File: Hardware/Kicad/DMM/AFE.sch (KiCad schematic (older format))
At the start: 4 parts

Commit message: Updated schematic file to include hierarchial schematic sheets for AFE and USB to FIFO subsystems
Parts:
- added C? (x2): SMD-CAP-100NF-0603, DBLS_Capacitor:C_0603_1608Metric_Pad1.05x0.95mm_HandSolder, symbol DBLS_Capacitor:SMD-CAP-100NF-0603
- added R? (x2): SMD-RES-0-0603, DBLS_Resistor:R_0603_1608Metric_Pad1.05x0.95mm_HandSolder, symbol DBLS_Resistor:SMD-RES-0-0603
- added U? (x2): AD8421, symbol DBLS_Amplifier:AD8421
- added U?: ADS7853, DBLS_QFN:QFN-16_EP_3.75x3.75_Pitch0.5mm, symbol DBLS_Data_Converters:ADS7853
- added U?: LT6237, DBLS_SOIC:MSOP-8_Pitch_0.65mm, symbol DBLS_Amplifier:LT6237
- added U?: OP2177, DBLS_SOIC:MSOP-8_Pitch_0.65mm, symbol DBLS_Amplifier:OP2177
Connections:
- net GND: now also C?.2, C?.2, U?.13 (GND)
- new net: C?.1, R?.2, U?.6 (REF) (x2)
- new net REF_A: R?.1, U?.1 (REFIO_A)
- new net REF_B: R?.1, U?.2 (REFGND-A)
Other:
- moved on the sheet: U?

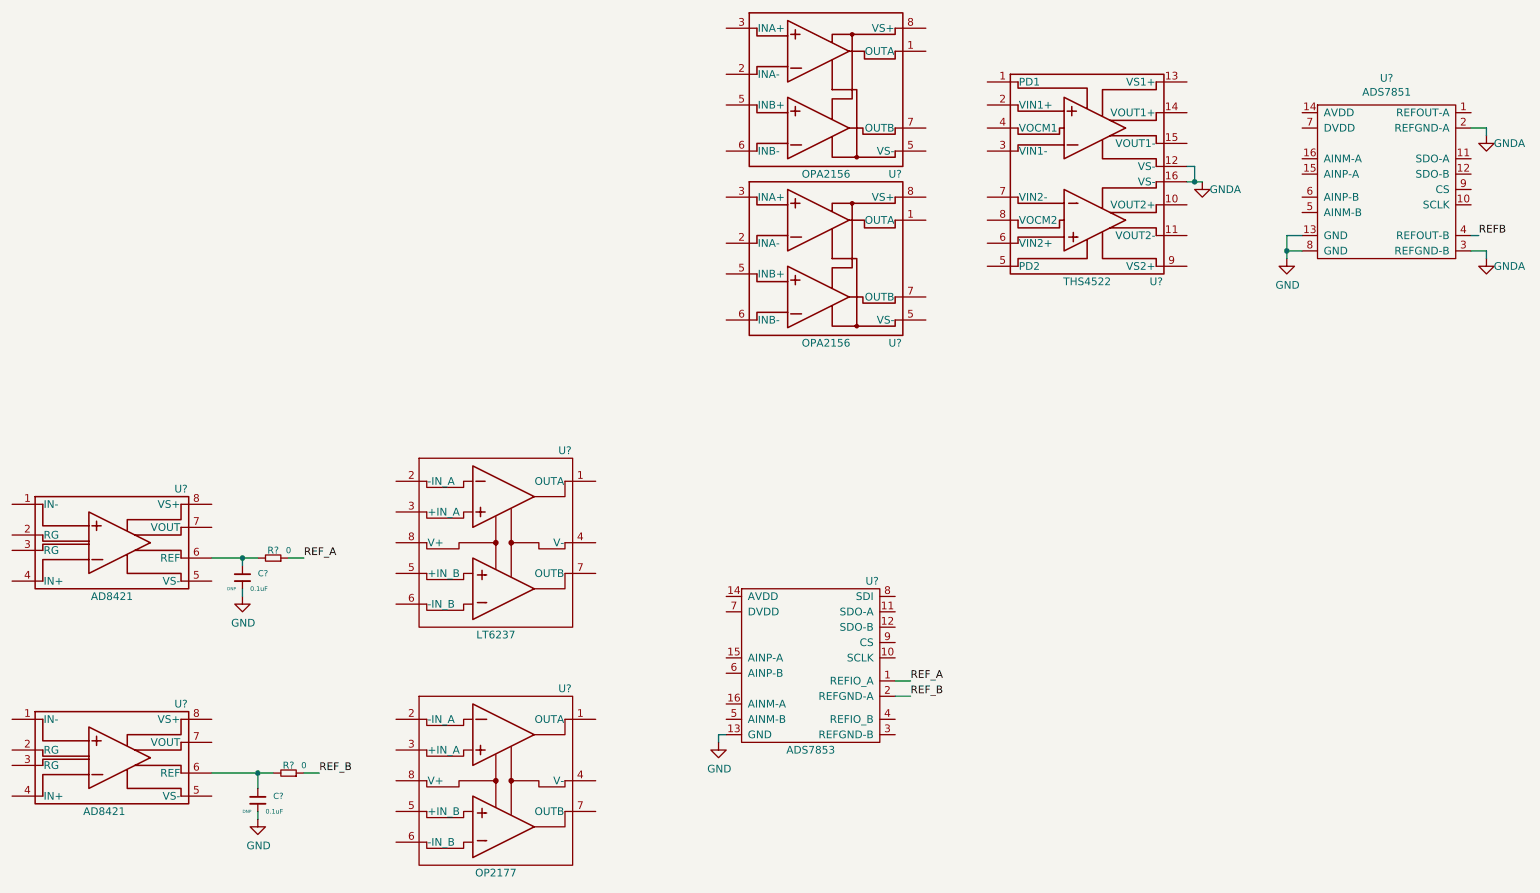
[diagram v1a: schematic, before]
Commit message: Continued AFE schematic developement, adding anti-alias filter, reference buffer, and gain stages.
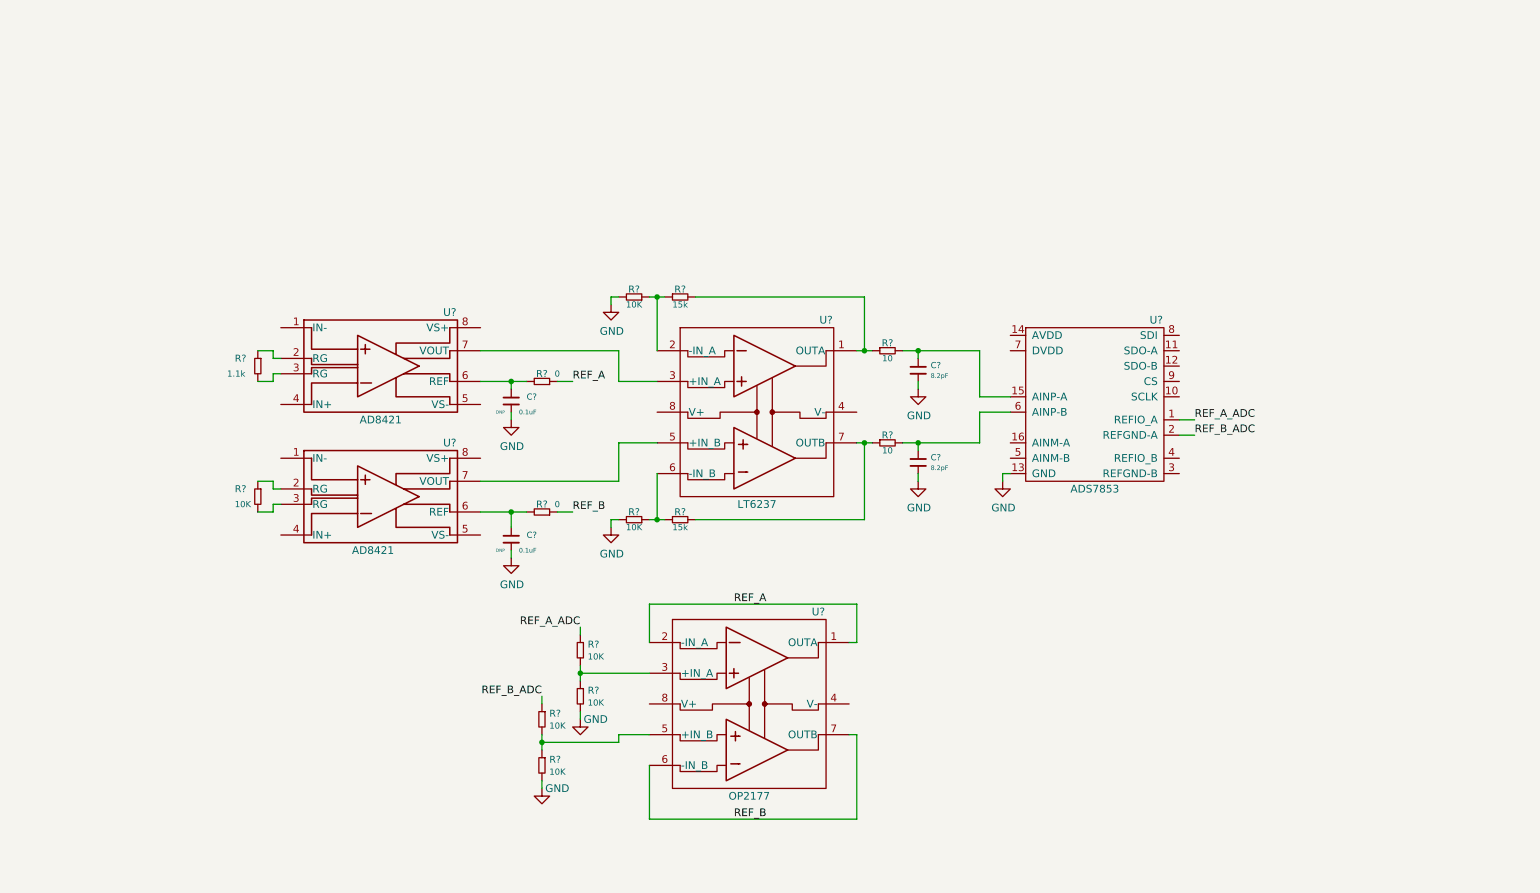
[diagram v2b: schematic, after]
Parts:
- removed U?: THS4522, symbol DBLS_Amplifier:THS4522
- removed U? (x2): OPA2156, symbol DBLS_Amplifier:OPA2156
- removed U?: ADS7851, DBLS_QFN:QFN-16_EP_3.75x3.75_Pitch0.5mm, symbol DBLS_Data_Converters:ADS7851
- removed U?: OP2177, DBLS_SOIC:MSOP-8_Pitch_0.65mm, symbol DBLS_Amplifier:OP2177
- added C? (x2): SMD-CAP-8.2PF-0603, DBLS_Capacitor:C_0603_1608Metric_Pad1.05x0.95mm_HandSolder, symbol DBLS_Capacitor:SMD-CAP-8.2PF-0603
- added R? (x7): SMD-RES-10K-0603-1TOL, DBLS_Resistor:R_0603_1608Metric_Pad1.05x0.95mm_HandSolder, symbol DBLS_Resistor:SMD-RES-10K-0603-1TOL
- added R?: SMD-RES-1.1K-0603, DBLS_Resistor:R_0603_1608Metric_Pad1.05x0.95mm_HandSolder, symbol DBLS_Resistor:SMD-RES-1.1K-0603-1TOL
- added R? (x2): SMD-RES-10-0603, DBLS_Resistor:R_0603_1608Metric_Pad1.05x0.95mm_HandSolder, symbol DBLS_Resistor:SMD-RES-10-0603
- added R? (x2): SMD-RES-15K-0603-1TOL, DBLS_Resistor:R_0603_1608Metric_Pad1.05x0.95mm_HandSolder, symbol DBLS_Resistor:SMD-RES-15K-0603-1TOL
- added U?: OP2177, DBLS_SOIC:MSOP-8_Pitch_0.65mm, symbol DBLS_Amplifier:OP2177
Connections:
- net GND: now also C?.2, C?.2, R?.2, R?.2, R?.2, R?.2
- net REF_A: now also U?.1 (OUTA), U?.2 (-IN_A); no longer U?.1 (REFIO_A)
- net REF_B: now also U?.6 (-IN_B), U?.7 (OUTB); no longer U?.2 (REFGND-A)
- net at U?.2 (RG): now also R?.1 (x2)
- net at U?.3 (RG): now also R?.2 (x2)
- net at U?.7 (VOUT): now also U?.3 (+IN_A)
- net at U?.15 (AINP-A): now also C?.1, R?.2
- net at U?.6 (AINP-B): now also C?.1, R?.2
- net at U?.7 (VOUT): now also U?.5 (+IN_B)
- net at U?.1 (OUTA): now also R?.1, R?.2
- net at U?.2 (-IN_A): now also R?.1, R?.1
- net at U?.6 (-IN_B): now also R?.1, R?.1
- net at U?.7 (OUTB): now also R?.1, R?.2
- new net: R?.1, R?.2, U?.3 (+IN_A)
- new net: R?.1, R?.2, U?.5 (+IN_B)
- new net REF_A_ADC: R?.1, U?.1 (REFIO_A)
- new net REF_B_ADC: R?.1, U?.2 (REFGND-A)
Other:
- moved on the sheet: C?, R?, U?
